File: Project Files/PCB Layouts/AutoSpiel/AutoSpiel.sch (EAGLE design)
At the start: 10 parts, among them Q1 TIP120

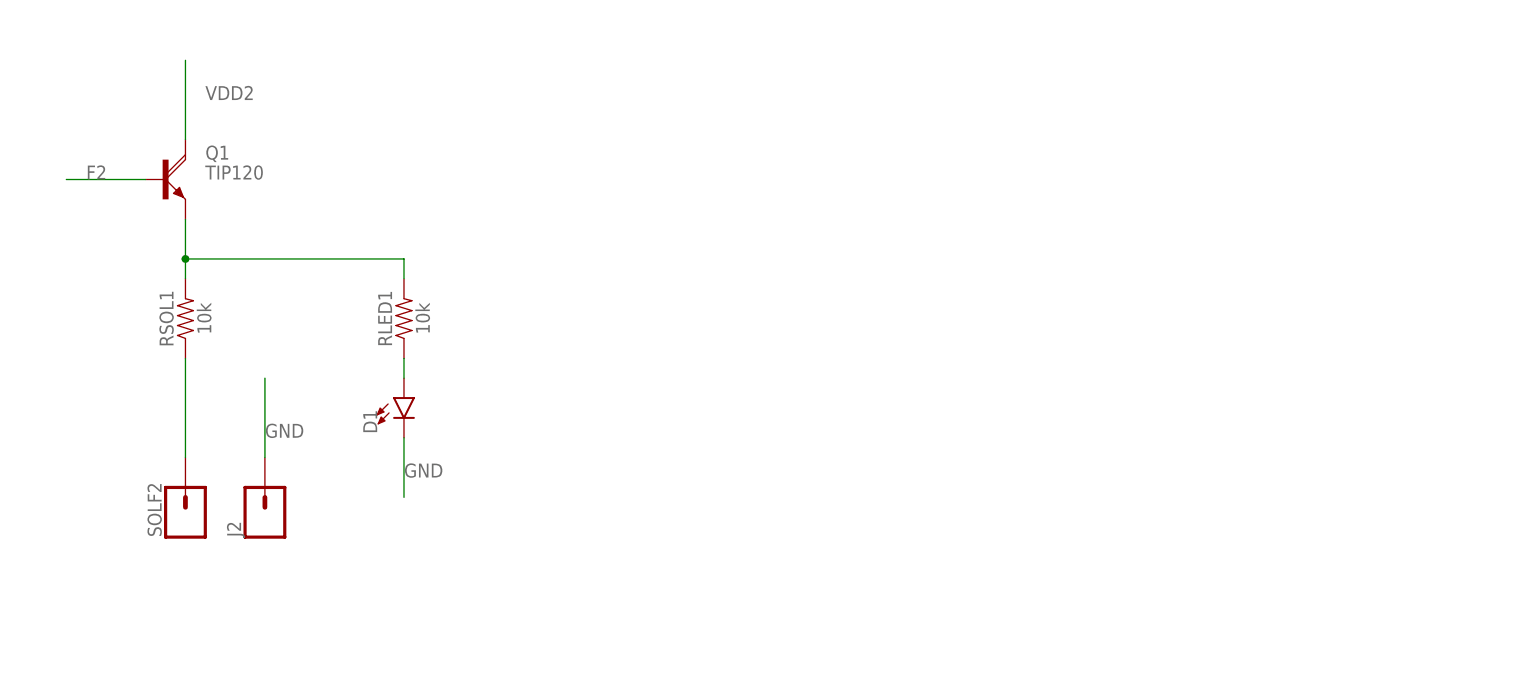
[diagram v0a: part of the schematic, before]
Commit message: Added more to the board to do fit testing
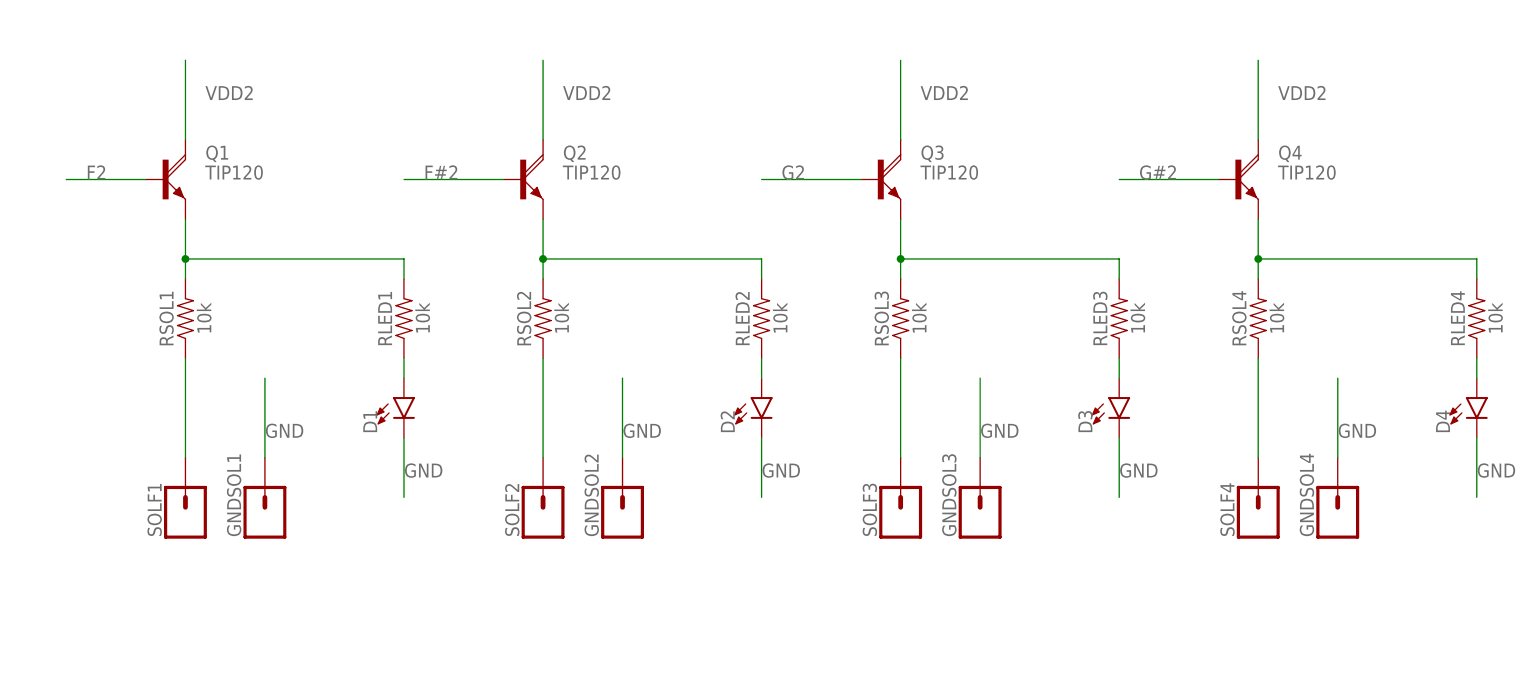
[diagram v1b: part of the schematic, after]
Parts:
- added D2, D3, D4: (no value), SparkFun-LED:LED3MM
- added GNDSOL2, GNDSOL3, GNDSOL4, SOLF1, SOLF3, SOLF4: (no value), SparkFun-Connectors:CONN_01
- added Q2, Q3, Q4: TIP120, transistor-power:TIP120
- added RLED2, RLED3, RLED4, RSOL2, RSOL3, RSOL4: 10k, SparkFun-Resistors:10KOHM-HORIZ_KIT-1/4W-5%
- renumbered J2 to GNDSOL1
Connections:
- new net N$1: Q2.E, RLED2.2, RSOL2.2
- new net N$10: D4.A, RLED4.1
- new net N$2: RSOL2.1, SOLF2.1
- new net N$3: D2.A, RLED2.1
- new net N$4: Q3.E, RLED3.2, RSOL3.2
- new net N$5: RSOL3.1, SOLF3.1
- new net N$7: D3.A, RLED3.1
- new net N$8: Q4.E, RLED4.2, RSOL4.2
- new net N$9: RSOL4.1, SOLF4.1
- net F#2: now also Q2.B
- net G#2: now also Q4.B
- net G2: now also Q3.B
- net GND: now also D2.C, D3.C, D4.C, GNDSOL2.1, GNDSOL3.1, GNDSOL4.1
- net N$37: now also SOLF1.1; no longer SOLF2.1
- net VDD2: now also Q2.C, Q3.C, Q4.C
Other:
- moved on the sheet: SOLF2

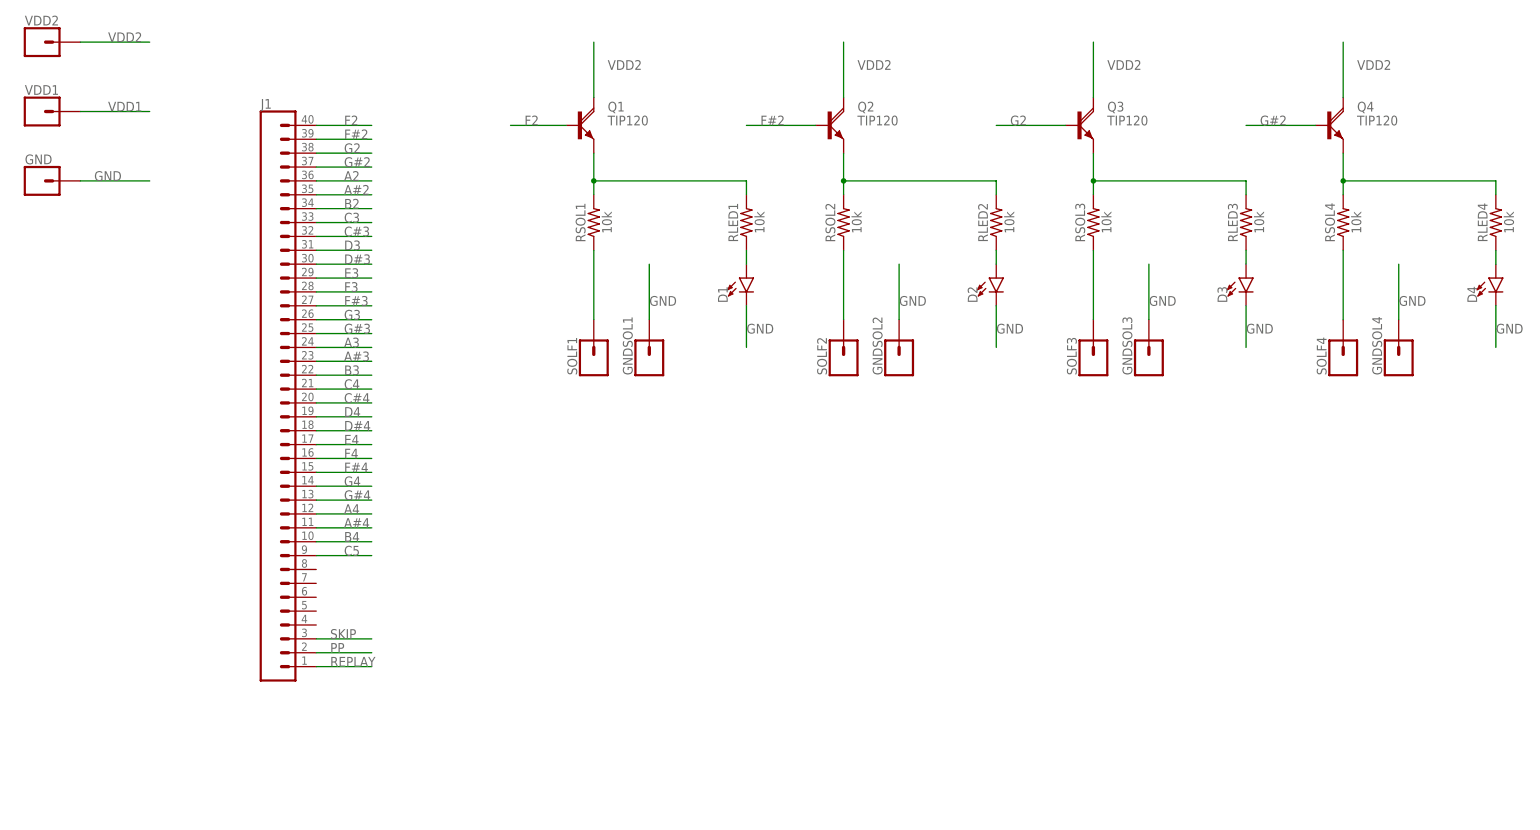
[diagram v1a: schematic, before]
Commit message: Added a couple of helpful pictures and redid the circuit based off of stuff I've researched
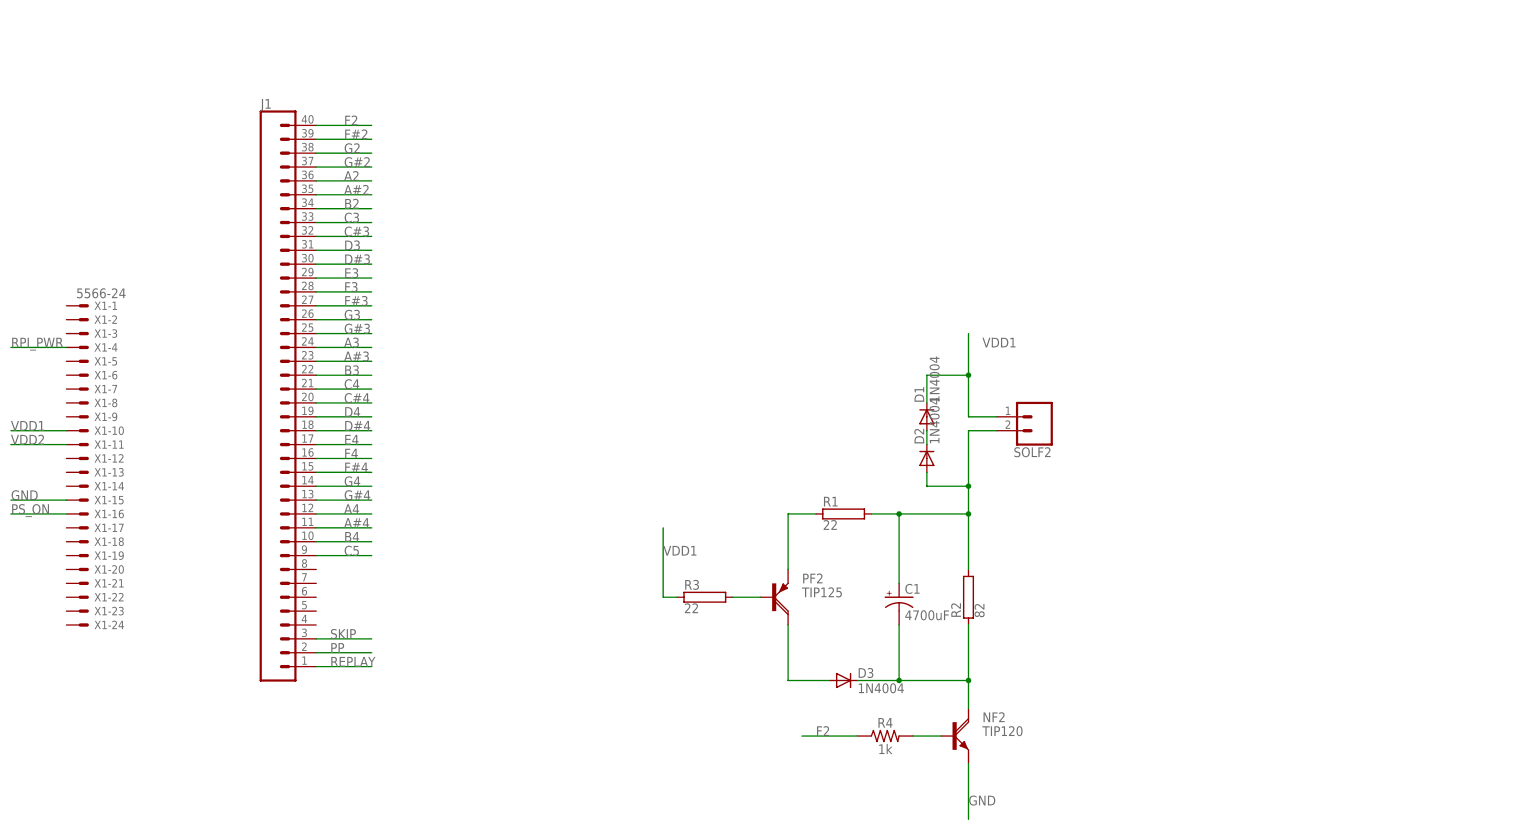
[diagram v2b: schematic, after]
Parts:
- removed D4: (no value), SparkFun-LED:LED3MM
- removed GND, GNDSOL1, GNDSOL2, GNDSOL3, GNDSOL4, SOLF1, SOLF3, SOLF4, VDD1, VDD2: (no value), SparkFun-Connectors:CONN_01
- removed Q1, Q2, Q3, Q4: TIP120, transistor-power:TIP120
- removed RLED1, RLED2, RLED3, RLED4, RSOL1, RSOL2, RSOL3, RSOL4: 10k, SparkFun-Resistors:10KOHM-HORIZ_KIT-1/4W-5%
- added C1: 4700uF, rcl:CPOL-USE5-13
- added NF2: TIP120, transistor-power:TIP120
- added PF2: TIP125, transistor-power:TIP125
- added R1, R3: 22, resistor-power:RAC01
- added R2: 82, resistor-power:RAC01
- added R4: 1k, SparkFun-Resistors:1KOHM-HORIZ_KIT-1/4W-5%
- added X1: 5566-24, con-molex:5566-24
- D1, D2, D3: value (none) -> 1N4004; device SparkFun-LED:LED3MM -> diode:1N4004
- SOLF2: device SparkFun-Connectors:CONN_01 -> SparkFun-Connectors:CONN_02PTH4
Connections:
- removed net N$10: D4.A, RLED4.1
- removed net N$2: RSOL2.1, SOLF2.1
- removed net N$37: RSOL1.1, SOLF1.1
- removed net N$38: D1.A, RLED1.1
- removed net N$6: Q1.E, RLED1.2, RSOL1.2
- removed net N$8: Q4.E, RLED4.2, RSOL4.2
- removed net N$9: RSOL4.1, SOLF4.1
- new net PS_ON: X1-16.S
- new net RPI_PWR: X1-4.S
- new net SOLGND1: C1.+, D2.A, R1.2, R2.2, SOLF2.2
- new net SOLGND2: PF2.B, R3.2
- net F#2: no longer Q2.B
- net F2: now also R4.1; no longer Q1.B
- net G#2: no longer Q4.B
- net G2: no longer Q3.B
- net GND: now also NF2.E, X1-15.S; no longer D1.C, D2.C, D3.C, D4.C, GND.1, GNDSOL1.1, GNDSOL2.1, GNDSOL3.1, GNDSOL4.1
- net N$1: now also NF2.B, R4.2; no longer Q2.E, RLED2.2, RSOL2.2
- net N$3: now also PF2.E, R1.1; no longer D2.A, RLED2.1
- net N$4: now also D3.A, PF2.C; no longer Q3.E, RLED3.2, RSOL3.2
- net N$5: now also C1.-, D3.C, NF2.C, R2.1; no longer RSOL3.1, SOLF3.1
- net N$7: now also D1.A, D2.C; no longer D3.A, RLED3.1
- net VDD1: now also D1.C, R3.1, SOLF2.1, X1-10.S; no longer VDD1.1
- net VDD2: now also X1-11.S; no longer Q1.C, Q2.C, Q3.C, Q4.C, VDD2.1
